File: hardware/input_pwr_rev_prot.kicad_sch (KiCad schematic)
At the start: 8 parts, among them U12 NTGS4111PT1G

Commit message: finalize revision of schematic
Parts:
- renumbered C10 to C8, C8 to C9, R21 to R1, U12 to U2
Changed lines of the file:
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@@
 		(dnp no)
 		(fields_autoplaced yes)
-		(property "Reference" "U12"
+		(property "Reference" "U2"
 			(at 120.65 83.82 0)
 			(effects
@@
 			(project "BREAD_Slice"
 				(path "/66043bca-a260-4915-9fce-8a51d324c687/2fc3e555-07d7-44ca-9332-cea1fde8760a"
-					(reference "U12")
+					(reference "U2")
 					(unit 1)
 				)
@@
 		(on_board yes)
 		(dnp no)
-		(property "Reference" "C10"
+		(property "Reference" "C8"
 			(at 161.036 95.504 0)
 			(effects
@@
 			(project "BREAD_Slice"
 				(path "/66043bca-a260-4915-9fce-8a51d324c687/2fc3e555-07d7-44ca-9332-cea1fde8760a"
-					(reference "C10")
+					(reference "C8")
 					(unit 1)
 				)
@@
 		(dnp no)
 		(fields_autoplaced yes)
-		(property "Reference" "R21"
+		(property "Reference" "R1"
 			(at 142.24 118.1099 0)
 			(effects
@@
 			(project "BREAD_Slice"
 				(path "/66043bca-a260-4915-9fce-8a51d324c687/2fc3e555-07d7-44ca-9332-cea1fde8760a"
-					(reference "R21")
+					(reference "R1")
 					(unit 1)
 				)
@@
 		(on_board yes)
 		(dnp no)
-		(property "Reference" "C8"
+		(property "Reference" "C9"
 			(at 173.99 95.25 0)
 			(effects
@@
 			(project "BREAD_Slice"
 				(path "/66043bca-a260-4915-9fce-8a51d324c687/2fc3e555-07d7-44ca-9332-cea1fde8760a"
-					(reference "C8")
-					(unit 1)
-				)
+					(reference "C9")
+					(unit 1)
+				)

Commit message: fix some footprint links
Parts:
- C7, C9: footprint (none) -> Capacitor_SMD:C_1206_3216Metric
- C8: footprint (none) -> Capacitor_SMD:CP_Elec_4x5.8
- NT2: footprint (none) -> NetTie:NetTie-2_SMD_Pad2.0mm
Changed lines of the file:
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@@
 			)
 		)
-		(property "Footprint" ""
+		(property "Footprint" "NetTie:NetTie-2_SMD_Pad2.0mm"
 			(at 109.22 128.27 0)
 			(effects
@@
 			)
 		)
-		(property "Footprint" ""
+		(property "Footprint" "Capacitor_SMD:CP_Elec_4x5.8"
 			(at 160.9852 104.14 0)
 			(effects
@@
 			)
 		)
-		(property "Footprint" ""
+		(property "Footprint" "Capacitor_SMD:C_1206_3216Metric"
 			(at 173.6852 104.14 0)
 			(effects
@@
 			)
 		)
-		(property "Footprint" ""
+		(property "Footprint" "Capacitor_SMD:C_1206_3216Metric"
 			(at 68.2752 124.46 0)
 			(effects

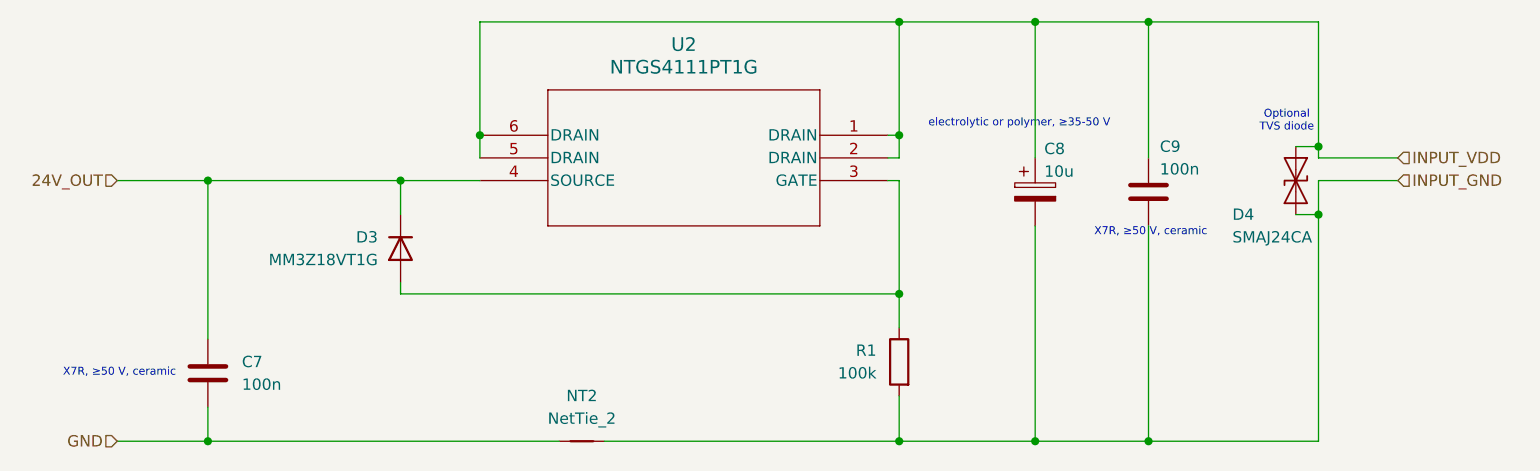
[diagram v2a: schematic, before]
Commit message: revision of symbol attachment and clear out old layout and start new; kml-custom to kmlib-local
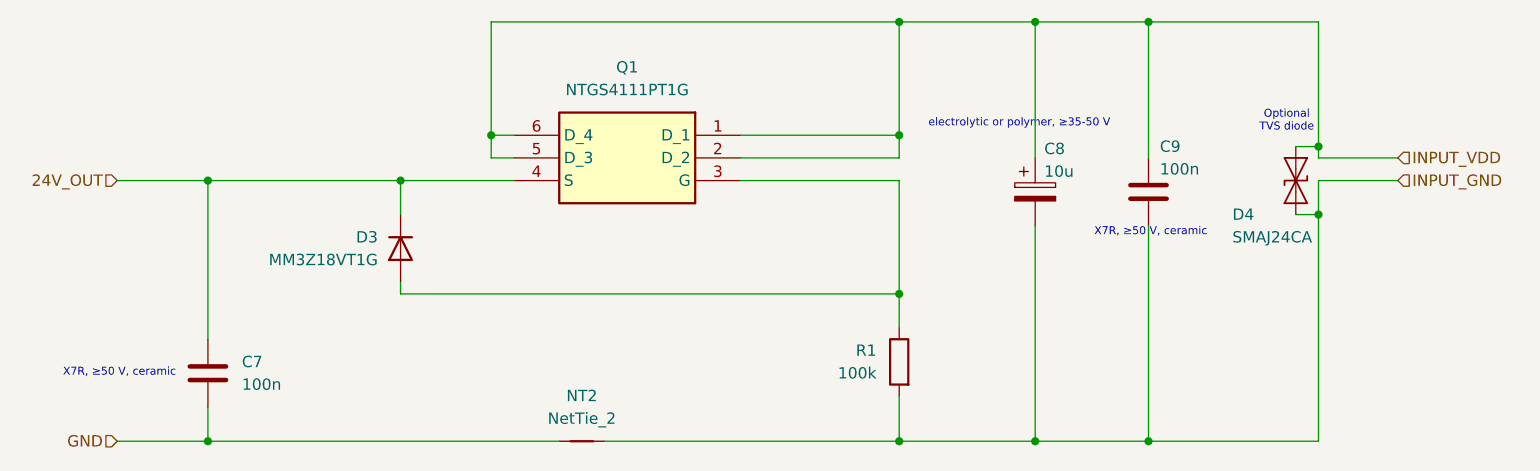
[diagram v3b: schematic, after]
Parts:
- removed U2: NTGS4111PT1G, TSOP6_3P1X1P7_ONS, symbol Transistor_FET:NTGS4111PT1G
- added Q1: NTGS4111PT1G, KMLib_IC_SMD:SOT95P275X110-6N, symbol KMLib_Discrete_Semiconductors:NTGS4111PT1G
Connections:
- net 24V_OUT: now also Q1.4 (S)
- net INPUT_VDD: now also Q1.1 (D_1), Q1.2 (D_2), Q1.5 (D_3), Q1.6 (D_4)
- net at D3.2 (A), R1.1: now also Q1.3 (G)
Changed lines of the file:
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@@
+	)
+	(junction
+		(at 99.06 93.98)
+		(diameter 0)
+		(color 0 0 0 0)
 	)
 	(junction
@@
 	)
 	(junction
-		(at 97.79 93.98)
-		(diameter 0)
-		(color 0 0 0 0)
-	)
-	(junction
 		(at 191.77 102.87)
 		(diameter 0)
@@
 	(wire
 		(pts
-			(xy 143.51 99.06) (xy 144.78 99.06)
+			(xy 127 99.06) (xy 144.78 99.06)
 		)
 		(stroke
@@
 	(wire
 		(pts
-			(xy 97.79 93.98) (xy 97.79 81.28)
-		)
-		(stroke
-			(width 0)
-			(type default)
-		)
-	)
-	(wire
-		(pts
 			(xy 189.23 95.25) (xy 191.77 95.25)
 		)
@@
 	(wire
 		(pts
-			(xy 97.79 93.98) (xy 97.79 96.52)
-		)
-		(stroke
-			(width 0)
-			(type default)
-		)
-	)
-	(wire
-		(pts
-			(xy 144.78 96.52) (xy 143.51 96.52)
+			(xy 99.06 81.28) (xy 99.06 93.98)
+		)
+		(stroke
+			(width 0)
+			(type default)
+		)
+	)
+	(wire
+		(pts
+			(xy 144.78 96.52) (xy 127 96.52)
 		)
 		(stroke
@@
 	(wire
 		(pts
-			(xy 88.9 99.06) (xy 97.79 99.06)
+			(xy 88.9 99.06) (xy 101.6 99.06)
 		)
 		(stroke
@@
 	(wire
 		(pts
-			(xy 144.78 93.98) (xy 143.51 93.98)
+			(xy 144.78 93.98) (xy 127 93.98)
 		)
 		(stroke
@@
 	(wire
 		(pts
-			(xy 144.78 81.28) (xy 97.79 81.28)
+			(xy 99.06 93.98) (xy 101.6 93.98)
+		)
+		(stroke
+			(width 0)
+			(type default)
+		)
+	)
+	(wire
+		(pts
+			(xy 144.78 81.28) (xy 99.06 81.28)
 		)
 		(stroke
@@
 		(pts
 			(xy 144.78 115.57) (xy 144.78 111.76)
+		)
+		(stroke
+			(width 0)
+			(type default)
+		)
+	)
+	(wire
+		(pts
+			(xy 99.06 93.98) (xy 99.06 96.52)
+		)
+		(stroke
+			(width 0)
+			(type default)
+		)
+	)
+	(wire
+		(pts
+			(xy 99.06 96.52) (xy 101.6 96.52)
 		)
 		(stroke
@@
 	)
 	(symbol
-		(lib_id "Transistor_FET:NTGS4111PT1G")
-		(at 143.51 93.98 0)
+		(lib_id "KMLib_Discrete_Semiconductors:NTGS4111PT1G")
+		(at 127 93.98 0)
 		(mirror y)
 		(unit 1)
@@
 		(on_board yes)
 		(dnp no)
-		(fields_autoplaced yes)
-		(property "Reference" "U2"
-			(at 120.65 83.82 0)
-			(effects
-				(font
-					(size 1.524 1.524)
+		(property "Reference" "Q1"
+			(at 114.3 86.36 0)
+			(effects
+				(font
+					(size 1.27 1.27)
 				)
 			)
 		)
 		(property "Value" "NTGS4111PT1G"
-			(at 120.65 86.36 0)
-			(effects
-				(font
-					(size 1.524 1.524)
-				)
-			)
-		)
-		(property "Footprint" "TSOP6_3P1X1P7_ONS"
-			(at 143.51 93.98 0)
-			(effects
-				(font
-					(size 1.27 1.27)
-					(italic yes)
-				)
-				(hide yes)
-			)
-		)
-		(property "Datasheet" "NTGS4111PT1G"
-			(at 143.51 93.98 0)
-			(effects
-				(font
-					(size 1.27 1.27)
-					(italic yes)
-				)
-				(hide yes)
-			)
-		)
-		(property "Description" ""
-			(at 143.51 93.98 0)
-			(effects
-				(font
-					(size 1.27 1.27)
-				)
-				(hide yes)
-			)
+			(at 114.3 88.9 0)
+			(effects
+				(font
+					(size 1.27 1.27)
+				)
+			)
+		)
+		(property "Footprint" "KMLib_IC_SMD:SOT95P275X110-6N"
+			(at 105.41 188.9 0)
+			(effects
+				(font
+					(size 1.27 1.27)
+				)
+				(justify left top)
+				(hide yes)
+			)
+		)
+		(property "Datasheet" "https://www.onsemi.com/pub/Collateral/NTGS4111P-D.PDF"
+			(at 105.41 288.9 0)
+			(effects
+				(font
+					(size 1.27 1.27)
+				)
+				(justify left top)
+				(hide yes)
+			)
+		)
+		(property "Description" "Leading -30 V, Trench Process for Low RDS(on); Low Profile Package Suitable for Portable Applications; Surface Mount TSOP-6 Saves Board Space; Improved Efficiency for Battery Applications"
+			(at 127 93.98 0)
+			(effects
+				(font
+					(size 1.27 1.27)
+				)
+				(hide yes)
+			)
+		)
+		(property "Height" "1.1"
+			(at 105.41 488.9 0)
+			(effects
+				(font
+					(size 1.27 1.27)
+				)
+				(justify left top)
+				(hide yes)
+			)
+		)
+		(property "Mouser Part Number" "863-NTGS4111PT1G"
+			(at 105.41 588.9 0)
+			(effects
+				(font
+					(size 1.27 1.27)
+				)
+				(justify left top)
+				(hide yes)
+			)
+		)
+		(property "Mouser Price/Stock" "https://www.mouser.co.uk/ProductDetail/onsemi/NTGS4111PT1G?qs=ZXBb0xZ9WeBFwyU7dgOqzw%3D%3D"
+			(at 105.41 688.9 0)
+			(effects
+				(font
+					(size 1.27 1.27)
+				)
+				(justify left top)
+				(hide yes)
+			)
+		)
+		(property "Manufacturer_Name" "onsemi"
+			(at 105.41 788.9 0)
+			(effects
+				(font
+					(size 1.27 1.27)
+				)
+				(justify left top)
+				(hide yes)
+			)
+		)
+		(property "Manufacturer_Part_Number" "NTGS4111PT1G"
+			(at 105.41 888.9 0)
+			(effects
+				(font
+					(size 1.27 1.27)
+				)
+				(justify left top)
+				(hide yes)
+			)
+		)
+		(pin "1"
+		)
+		(pin "3"
 		)
 		(pin "2"
 		)
-		(pin "1"
+		(pin "5"
+		)
+		(pin "6"
 		)
 		(pin "4"
 		)
-		(pin "5"
-		)
-		(pin "6"
-		)
-		(pin "3"
-		)
 		(instances
-			(project "BREAD_Slice"
+			(project ""
 				(path "/66043bca-a260-4915-9fce-8a51d324c687/2fc3e555-07d7-44ca-9332-cea1fde8760a"
-					(reference "U2")
+					(reference "Q1")
 					(unit 1)
 				)
